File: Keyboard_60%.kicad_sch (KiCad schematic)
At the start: 36 parts, among them J3 Prog_conn, J5 Tag connect TC2030-CTX, U3 NRF52840-QIAA-R, Y1 32MHz, Y2 32.768kHz

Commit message: Pcb routing complete
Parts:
- added R3 (x5): 10k, keyboard:R_0402_1005Metric, symbol keyboard:R_US
- U3: MANUFACTURER (none) -> NORDIC Semiconductor; MAXIMUM_PACKAGE_HIEGHT (none) -> 0.85mm; STANDARD (none) -> Manufacturer Recommendations
- Y1: LCSC Part Number (none) -> C5261236
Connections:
- net nReset is gone; now on net ~{nReset}: J5.3 (Pin_3)
- net 3V3: no longer J5.1 (Pin_1)
- net COL0: now also U3.U24 (P1.04)
- net COL1: now also U3.W24 (P1.02)
- net COL10: now also U3.J1 (P0.04/AIN2)
- net COL11: now also U3.G1 (P0.26)
- net COL12: now also U3.A8 (P0.31/AIN7)
- net COL13: now also U3.A10 (P0.29/AIN5)
- net COL14: now also U3.A14 (P1.15)
- net COL2: now also U3.AD20 (P0.24)
- net COL3: now also U3.AD18 (P0.22)
- net COL4: now also U3.AD16 (P0.20)
- net COL5: now also U3.AD10 (P0.15)
- net COL6: now also U3.AD8 (P0.13)
- net COL7: now also U3.R1 (P1.09/TRACEDATA3)
- net COL8: now also U3.N1 (P0.08)
- net COL9: now also U3.L1 (P0.06)
- net ROW0: now also U3.A20 (P1.10), R3.2
- net ROW1: now also U3.A16 (P1.13), R3.2
- net ROW2: now also U3.J24 (P0.10/NFC2), R3.2
- net ROW3: now also U3.L24 (P0.09/NFC1), R3.2
- net ROW4: now also U3.R24 (P1.06), R3.2
- net ~{nReset}: now also U3.AD12 (P0.17)
- net ANT_FEED: now reaches AE1.1 (A), C11.1, L1.2
- net at JP1.2 (B), R3.2, R3.2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: now also J5.1 (Pin_1)
- new net switch_matrix/ROW0: R3.1
- new net switch_matrix/ROW1: R3.1
- new net switch_matrix/ROW2: R3.1
- new net switch_matrix/ROW3: R3.1
- new net switch_matrix/ROW4: R3.1
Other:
- moved on the sheet: C11

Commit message: Completed routing and solved DRC
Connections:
- net DB_SWDIO: now also J3.6 (Pin_6); no longer J3.3 (Pin_3)
- net DB_SWO: now also J3.2 (Pin_2); no longer J3.5 (Pin_5)
- net GND: now also J3.5 (Pin_5); no longer J3.4 (Pin_4)
- net VDD_nRF: now also J3.10 (Pin_10), JP1.1 (A)
- removed net 3V3: J3.2 (Pin_2), JP1.1 (A)
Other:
- moved on the sheet: J3, J5, JP1, R3

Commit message: gerber generated
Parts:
- removed R4 (x2): 22E, keyboard:R_0402_1005Metric, symbol keyboard:R_US
- C5, C6, C7, C8: value 100nF -> 8pF; LCSC Part Number C1525 -> C962144; LCSC link https://www.lcsc.com/product-detail/Multilayer-Ceramic-Capacitors-MLCC-SMD-SMT_Samsung-Electro-Mechanics-CL05B104KO5NNNC_C1525.html -> https://www.lcsc.com/product-detail/Multilayer-Ceramic-Capacitors-MLCC-SMD-SMT_YAGEO-CC0201CRNPO8BN8R0_C5182411.html; PN CL05B104KO5NNNC -> AC0402CRNPO9BN8R0
- L1: LCSC Part Number C5201661 -> C136252; LCSC link https://www.lcsc.com/product-detail/Inductors-SMD_Chilisin-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 -> https://www.lcsc.com/product-detail/Inductors-SMD_TDK-MLK10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; PN BSCH001005054N7SCS -> MLK1005S4N7ST000
- U3: value NRF52840-QIAA-R -> nRF52840-QIAA-R/nRF52833-QIAA-R; LCSC Part Number C190794 -> C190794, C504799; LCSC link https://www.lcsc.com/product-detail/RF-Transceiver-ICs_Nordic-Semicon-NRF52840-QIAA-R_C190794.html -> https://www.lcsc.com/product-detail/RF-Transceiver-ICs_Nordic-Semicon-NRF52840-QIAA-R_C190794.html, https://www.lcsc.com/product-detail/RF-Transceiver-ICs_Nordic-Semicon-nRF52833-QIAA-R_C504799.html; MANUFACTURER NORDIC Semiconductor -> (none); MAXIMUM_PACKAGE_HIEGHT 0.85mm -> (none); PN NRF52840-QIAA-R -> nRF52840-QIAA-R, nRF52833-QIAA-R; STANDARD Manufacturer Recommendations -> (none)
- Y1: LCSC Part Number C5261236 -> C2149125; LCSC link https://www.lcsc.com/product-detail/Crystals_Lucki-L327S320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 -> https://www.lcsc.com/product-detail/Crystals_JYJE-3TJ432000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; PN C5261236 -> 3TJ432000HYFBC
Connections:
- net USB_D+: now also U3.AD6 (D+)
- net USB_D-: now also U3.AD4 (D-)
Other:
- note added: "In the schematic, nRF52840 is shown. But it can be swapped out for nRF52840 without any changes. Its plug and play."
- note added: "Keyboard is designed in such a way that it is compatible with nRF52833 and nrf52840. Since these both are pin to pin compatible and some pins thatb are NC in nRF52833 are not utilized in the design making it compatible with both MCU's."

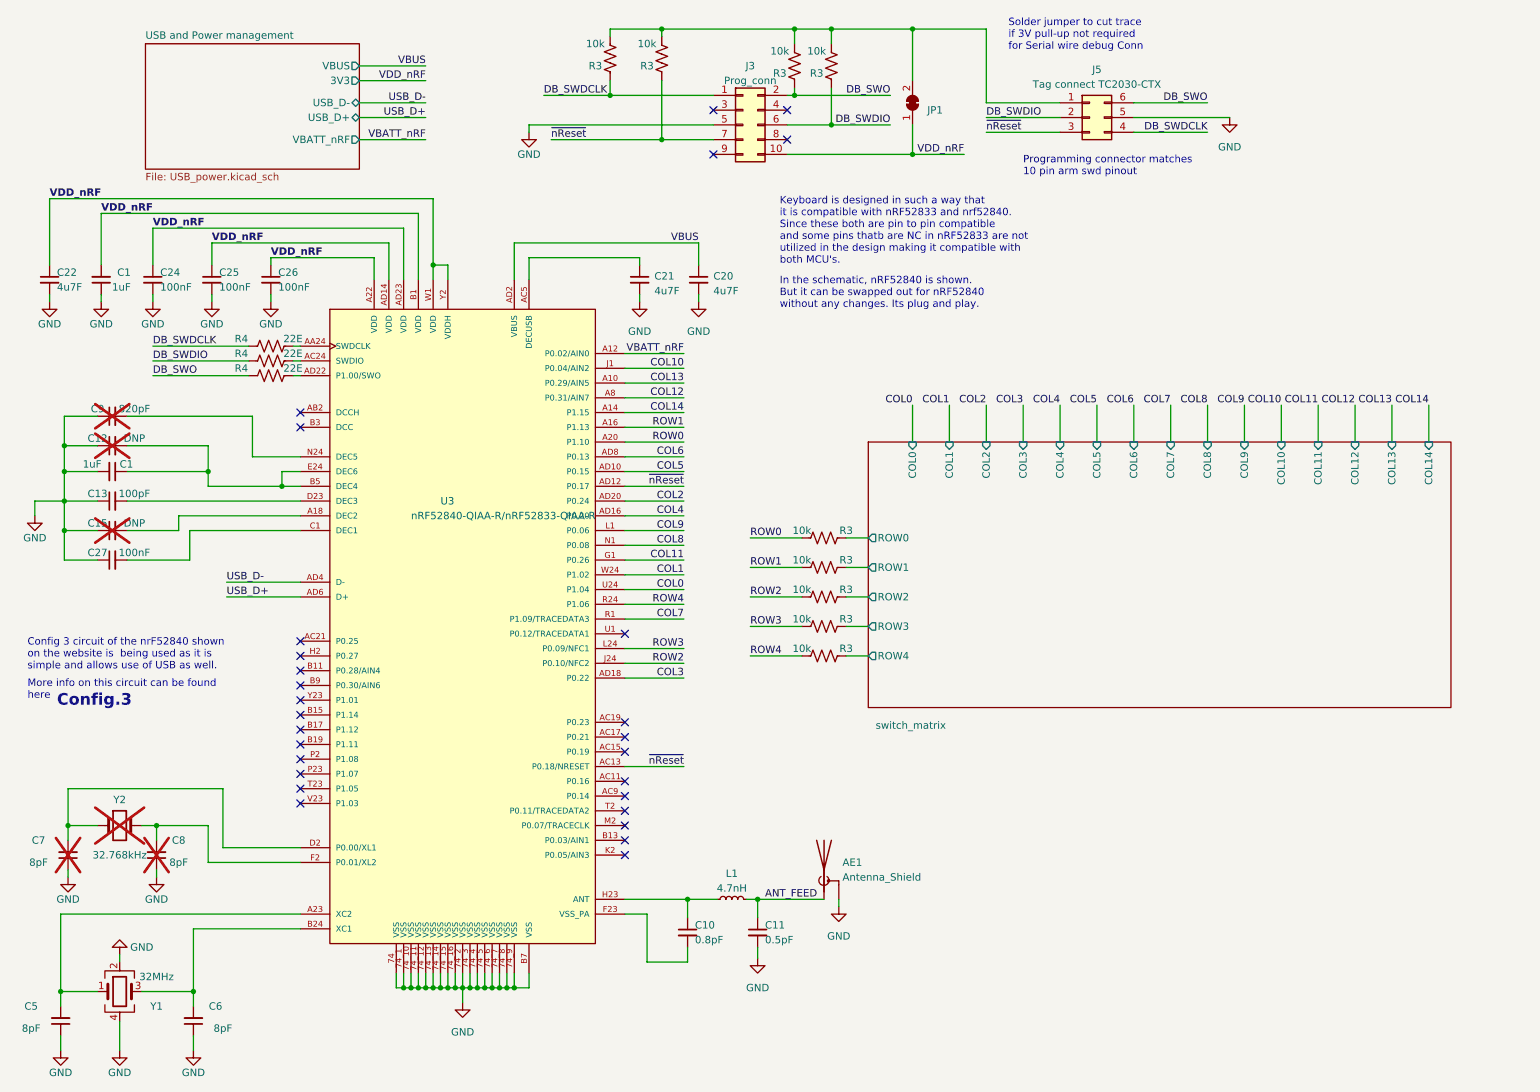
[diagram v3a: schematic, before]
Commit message: Made changes to add support for salvation keyboard case and discord reviews implemented
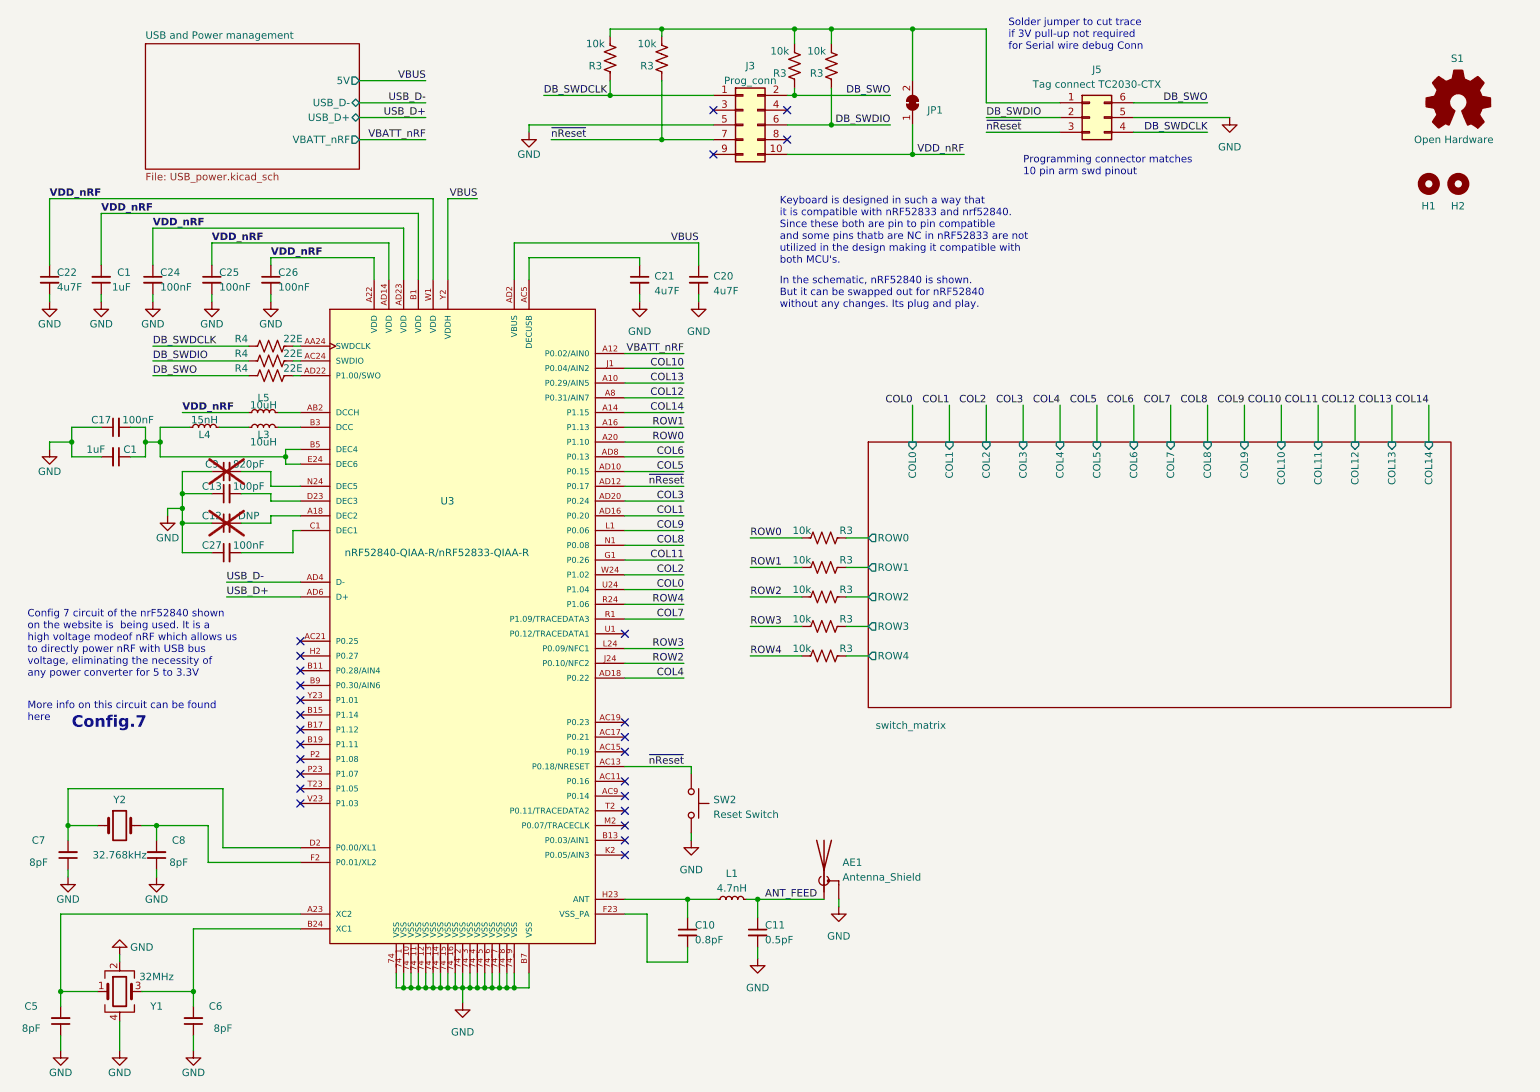
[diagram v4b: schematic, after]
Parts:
- removed C15: DNP, keyboard:C_0402_1005Metric, symbol keyboard:C_Small
- added C17: 100nF, keyboard:C_0402_1005Metric, symbol keyboard:C_Small
- added H1, H2: MountingHole, keyboard:salvation_mounting_holes, symbol keyboard:MountingHole
- added L3, L5: 10uH, keyboard:L_0603_1608Metric, symbol keyboard:L_Small
- added L4: 15nH, keyboard:L_0402_1005Metric, symbol keyboard:L_Small
- added S1: Open Hardware, keyboard:OSHW-Logo, symbol keyboard:Logo_Open_Hardware_Small
- added SW2: Reset Switch, keyboard:RST_SW, symbol keyboard:SW_Push
- C7, C8: now fitted; now in the parts list
- U3: MANUFACTURER (none) -> NORDIC Semiconductor; MAXIMUM_PACKAGE_HIEGHT (none) -> 0.85mm; STANDARD (none) -> Manufacturer Recommendations
- Y2: LCSC Part Number C5116075 -> C97605; LCSC link https://www.lcsc.com/product-detail/Crystals_TAE-Zhejiang-A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 -> https://www.lcsc.com/product-detail/Crystals_Seiko-SC-32S32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; PN TNXM32768K2NQDCZT2T -> SC-32S32.768kHz20PPM9pF; now fitted; now in the parts list
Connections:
- net COL1: now also U3.AD16 (P0.20); no longer U3.W24 (P1.02)
- net COL2: now also U3.W24 (P1.02); no longer U3.AD20 (P0.24)
- net COL3: now also U3.AD20 (P0.24); no longer U3.AD18 (P0.22)
- net COL4: now also U3.AD18 (P0.22); no longer U3.AD16 (P0.20)
- net GND: now also C17.1, SW2.2
- net VBUS: now also U3.Y2 (VDDH)
- net VDD_nRF: now also L5.1; no longer U3.Y2 (VDDH)
- net ~{nReset}: now also SW2.1
- net at U3.A18 (DEC2): now also C12.2
- net at C1.1, U3.B5 (DEC4), U3.E24 (DEC6): now also C17.2, L4.1; no longer C12.2
- net at U3.AB2 (DCCH): now also L5.2
- net at U3.B3 (DCC): now also L3.2
- new net: L3.1, L4.2
- no-connect marks 28 -> 26
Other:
- sheet USB and Power management ports: added 5V; removed 3V3, VBUS
- note added: "Config 7 circuit of the nrF52840 shown on the website is being used. It is a high voltage modeof nRF which allows us to directly power nRF with USB bus voltage, eliminating the necessity of any power converter for 5 to 3.3V"
- note added: "Config.7"
- note removed: "Config 3 circuit of the nrF52840 shown on the website is being used as it is simple and allows use of USB as well."
- note removed: "Config.3"
- moved on the sheet: C1, C12, C13, C27, C9

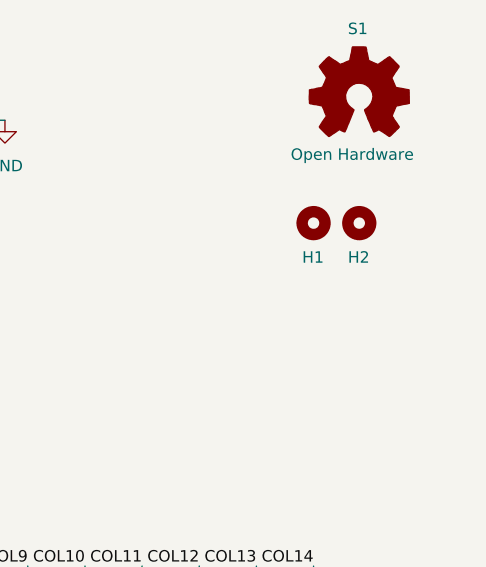
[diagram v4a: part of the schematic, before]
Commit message: Added mounting holes for tray mount style
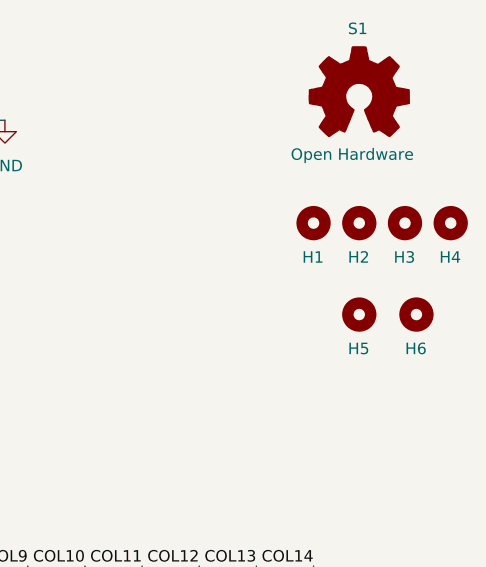
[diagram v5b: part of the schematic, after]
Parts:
- added H3, H4: MountingHole, keyboard:salvation_mounting_holes, symbol keyboard:MountingHole
- added H5, H6: MountingHole, keyboard:PKRHSL, symbol keyboard:MountingHole
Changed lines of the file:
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@@
+    )
+  )
+  (symbol (lib_id "keyboard:MountingHole") (at 273.05 43.18 0) (unit 1)
+    (in_bom no) (on_board yes) (dnp no)
+    (property "Reference" "H4" (at 271.78 46.99 0)
+      (effects (font (size 1.27 1.27)) (justify left))
+    )
+    (property "Value" "MountingHole" (at 275.59 45.085 0)
+      (effects (font (size 1.27 1.27)) (justify left) hide)
+    )
+    (property "Footprint" "keyboard:salvation_mounting_holes" (at 273.05 43.18 0)
+      (effects (font (size 1.27 1.27)) hide)
+    )
+    (property "Datasheet" "~" (at 273.05 43.18 0)
+      (effects (font (size 1.27 1.27)) hide)
+    )
+    (property "Sim.Enable" "0" (at 273.05 43.18 0)
+      (effects (font (size 1.27 1.27)) hide)
+    )
+    (instances
+      (project "Keyboard_60%"
+        (path "/ef112b03-6536-453f-8127-17d1495b48aa"
+          (reference "H4") (unit 1)
+        )
+      )
     )
   )
@@
         (path "/ef112b03-6536-453f-8127-17d1495b48aa"
           (reference "C25") (unit 1)
+        )
+      )
+    )
+  )
+  (symbol (lib_id "keyboard:MountingHole") (at 262.89 53.34 0) (unit 1)
+    (in_bom no) (on_board yes) (dnp no)
+    (property "Reference" "H5" (at 261.62 57.15 0)
+      (effects (font (size 1.27 1.27)) (justify left))
+    )
+    (property "Value" "MountingHole" (at 265.43 55.245 0)
+      (effects (font (size 1.27 1.27)) (justify left) hide)
+    )
+    (property "Footprint" "keyboard:PKRHSL" (at 262.89 53.34 0)
+      (effects (font (size 1.27 1.27)) hide)
+    )
+    (property "Datasheet" "~" (at 262.89 53.34 0)
+      (effects (font (size 1.27 1.27)) hide)
+    )
+    (property "Sim.Enable" "0" (at 262.89 53.34 0)
+      (effects (font (size 1.27 1.27)) hide)
+    )
+    (instances
+      (project "Keyboard_60%"
+        (path "/ef112b03-6536-453f-8127-17d1495b48aa"
+          (reference "H5") (unit 1)
         )
       )
@@
     )
   )
+  (symbol (lib_id "keyboard:MountingHole") (at 267.97 43.18 0) (unit 1)
+    (in_bom no) (on_board yes) (dnp no)
+    (property "Reference" "H3" (at 266.7 46.99 0)
+      (effects (font (size 1.27 1.27)) (justify left))
+    )
+    (property "Value" "MountingHole" (at 270.51 45.085 0)
+      (effects (font (size 1.27 1.27)) (justify left) hide)
+    )
+    (property "Footprint" "keyboard:salvation_mounting_holes" (at 267.97 43.18 0)
+      (effects (font (size 1.27 1.27)) hide)
+    )
+    (property "Datasheet" "~" (at 267.97 43.18 0)
+      (effects (font (size 1.27 1.27)) hide)
+    )
+    (property "Sim.Enable" "0" (at 267.97 43.18 0)
+      (effects (font (size 1.27 1.27)) hide)
+    )
+    (instances
+      (project "Keyboard_60%"
+        (path "/ef112b03-6536-453f-8127-17d1495b48aa"
+          (reference "H3") (unit 1)
+        )
+      )
+    )
+  )
   (symbol (lib_id "keyboard:MountingHole") (at 257.81 43.18 0) (unit 1)
     (in_bom no) (on_board yes) (dnp no)
@@
         )
       )
+    )
+  )
+  (symbol (lib_id "keyboard:MountingHole") (at 269.24 53.34 0) (unit 1)
+    (in_bom no) (on_board yes) (dnp no)
+    (property "Reference" "H6" (at 267.97 57.15 0)
+      (effects (font (size 1.27 1.27)) (justify left))
+    )
+    (property "Value" "MountingHole" (at 271.78 55.245 0)
+      (effects (font (size 1.27 1.27)) (justify left) hide)
+    )
+    (property "Footprint" "keyboard:PKRHSL" (at 269.24 53.34 0)
+      (effects (font (size 1.27 1.27)) hide)
+    )
+    (property "Datasheet" "~" (at 269.24 53.34 0)
+      (effects (font (size 1.27 1.27)) hide)
+    )
+    (property "Sim.Enable" "0" (at 269.24 53.34 0)
+      (effects (font (size 1.27 1.27)) hide)
+    )
+    (instances
+      (project "Keyboard_60%"
+        (path "/ef112b03-6536-453f-8127-17d1495b48aa"
+          (reference "H6") (unit 1)
+        )
+      )
